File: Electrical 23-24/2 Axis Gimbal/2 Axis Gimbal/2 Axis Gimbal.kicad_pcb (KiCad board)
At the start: 2 copper layers, 29 parts, among them IC1 BNO085, IC2 AP1086DL-13, J1 Conn_01x06_Socket, J2 Conn_01x06_Socket, U1 ATtiny404-SS

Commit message: Starteddddd
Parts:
- removed I2C1: Conn_01x02_Socket, Connector_PinSocket_2.54mm:PinSocket_1x02_P2.54mm_Vertical
- moved IC1 84.3 mm to (92.6, 90.0)
- moved U1 83.8 mm to (92.8, 101.1), turned to 90 degrees
- moved IC2 62.5 mm to (100.8, 111.2), turned to 180 degrees
- moved Power1 29.6 mm to (106.2, 110.5), turned to 180 degrees
- moved XTAL1 25.2 mm to (101.0, 86.8), turned to 90 degrees
- moved J2 22.3 mm to (106.2, 85.4)
- moved Servo2 22.2 mm to (89.6, 113.0), turned to 90 degrees
- moved UART1 19.7 mm to (106.2, 101.8)
- moved Servo1 18.4 mm to (89.6, 109.4), turned to 90 degrees
- moved UDPI1 14.2 mm to (84.0, 106.4), turned to 180 degrees
- moved D-CUP2 14.2 mm to (89.1, 89.5), turned to 90 degrees
- moved D-CUP3 12.7 mm to (93.1, 85.8)
- moved R5 12.7 mm to (88.0, 93.2), turned to 180 degrees
- moved C1 11.9 mm to (87.0, 101.3), turned to 90 degrees
- moved R4 11.6 mm to (92.9, 95.5), turned to 90 degrees
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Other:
- board outline added: 45 x 45 mm

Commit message: Update 2 Axis Gimbal.kicad_pcb
Finished PCB
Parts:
- moved Power1 28.5 mm to (77.9, 107.3)
- moved D1 22.2 mm to (83.2, 85.0)
- moved R3 21.5 mm to (78.2, 83.8), turned to 180 degrees
- moved C5 21.4 mm to (78.2, 94.8)
- moved R55 20.3 mm to (88.5, 86.8), turned to 90 degrees
- moved R4 20.1 mm to (78.2, 81.8), turned to 0 degrees
- moved IC2 18.6 mm to (83.2, 105.0)
- moved J2 17.8 mm to (92.0, 74.7)
- moved R5 17.0 mm to (78.7, 79.0)
- moved R2 16.8 mm to (78.7, 77.5)
- moved D-CUP1 16.2 mm to (86.4, 76.0), turned to 180 degrees
- moved R6 16.0 mm to (87.8, 82.0)
- moved XTAL1 15.7 mm to (89.0, 76.7)
- moved D-CUP2 15.5 mm to (81.5, 76.0), turned to 180 degrees
- moved C3 15.2 mm to (87.0, 79.9)
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- renumbered Servo1 to Serv1, Servo2 to Serv2
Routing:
- net 3.3: track 0.00 -> 90.0 mm, vias 0 -> 10
- net GND: track 0.00 -> 58.8 mm, vias 0 -> 4
- net STAT: track 0.00 -> 32.0 mm, vias 0 -> 2
- net CSN: track 0.00 -> 18.4 mm, vias 0 -> 2
- net SCL: track 0.00 -> 18.1 mm, vias 0 -> 2
- net RST: track 0.00 -> 17.6 mm, vias 0 -> 2
- net SDA: track 0.00 -> 17.0 mm, vias 0 -> 2
- net RX: track 0.00 -> 16.3 mm
- net INT: track 0.00 -> 16.1 mm, vias 0 -> 2
- net +BATT: track 0.00 -> 15.3 mm
- net PWM 2: track 0.00 -> 14.9 mm
- net TX: track 0.00 -> 14.3 mm
- net PWM 1: track 0.00 -> 13.5 mm
- net UPDI: track 0.00 -> 12.2 mm
- net BOOTN: track 0.00 -> 12.1 mm, vias 0 -> 2
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- added copper zone on F.Cu, net (none)
- added copper zone on B.Cu, net GND
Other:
- board size 45 x 45 mm -> 24.2 x 38.5 mm

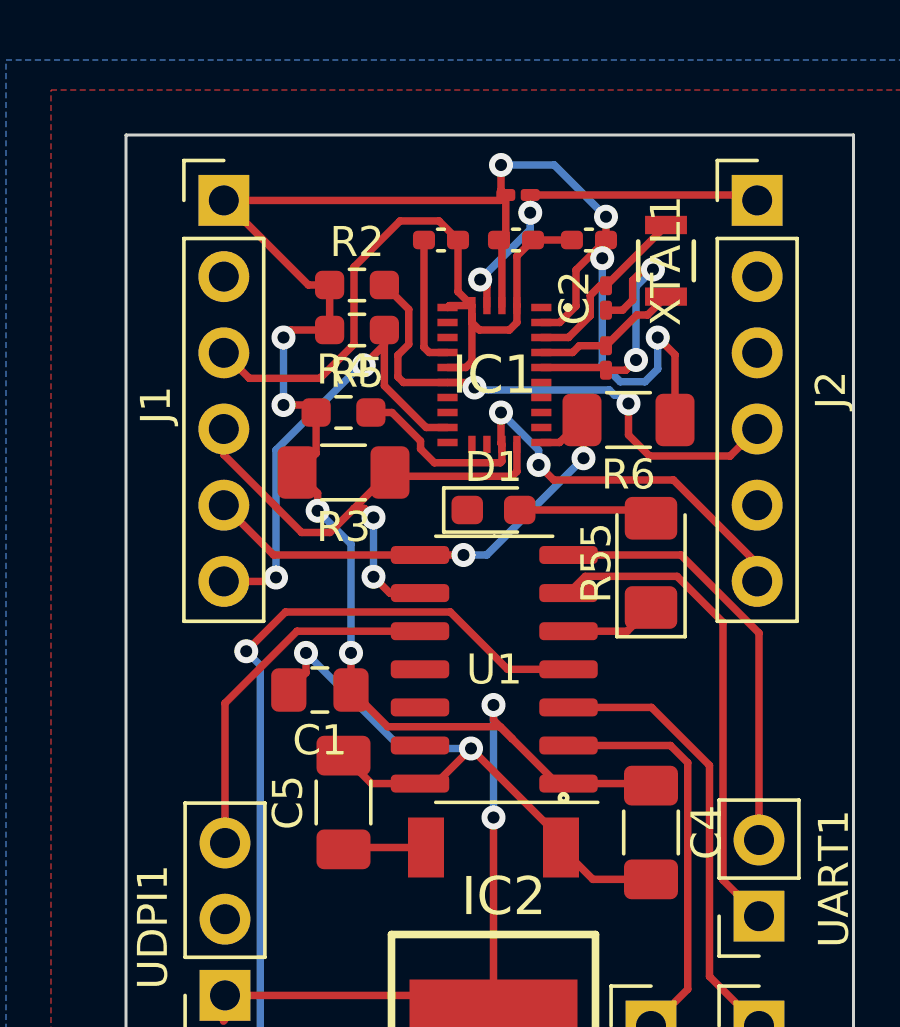
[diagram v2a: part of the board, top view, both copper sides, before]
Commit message: Reformatted PCB
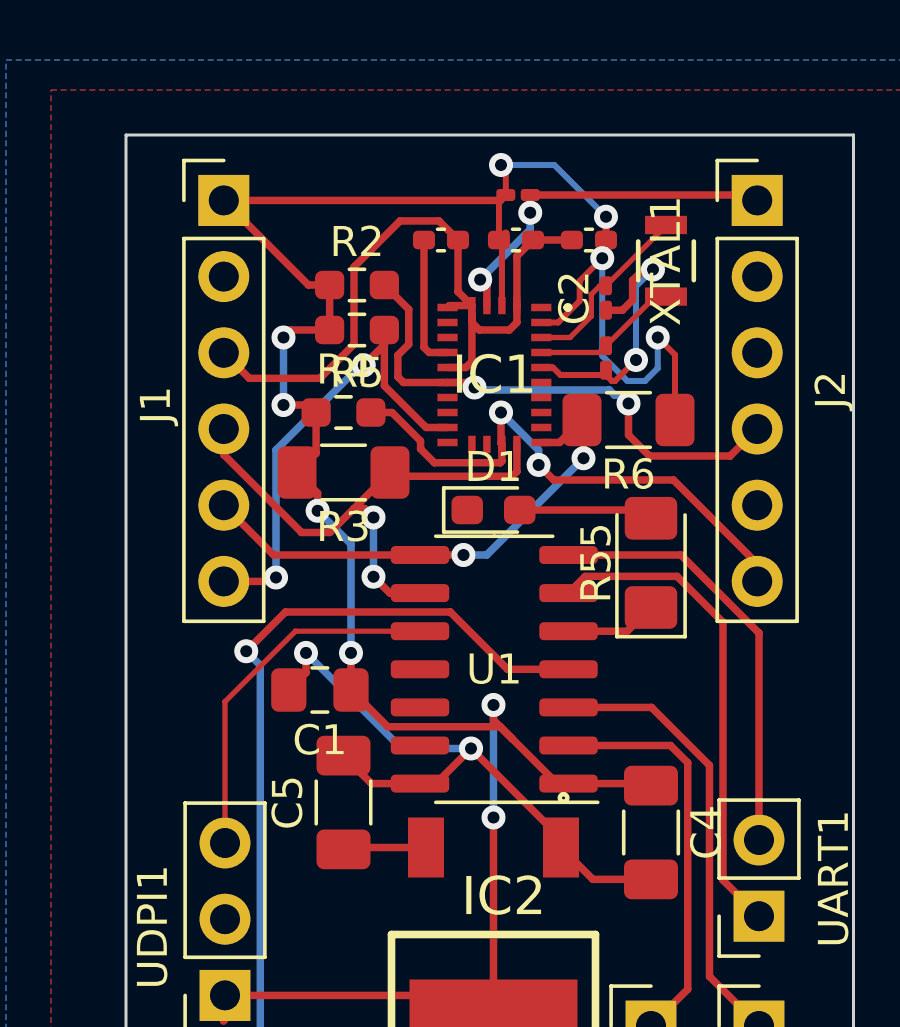
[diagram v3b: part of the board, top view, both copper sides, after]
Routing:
- net GND: track 58.8 -> 59.4 mm
- net 3.3: track 90.0 -> 89.4 mm

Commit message: Finished Gimbal Board
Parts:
- removed the C2 at (87.0, 77.9)
- removed the C3 at (87.0, 79.9)
- removed J1, J2: Conn_01x06_Socket, Connector_PinHeader_2.54mm:PinHeader_1x06_P2.54mm_Vertical
- removed XTAL1: ABS07-32.768KHZ-7-T, 32Crys:XTAL_ABS07-32.768KHZ-7-T_ABR
- added G***: LOGO, LOGO, B.Cu at (108.1, 81.3)
- added R7: 2.2k, Resistor_SMD:R_0603_1608Metric_Pad0.98x0.95mm_HandSolder, F.Cu at (112.9, 85.6)
- added Servo3: Conn_01x03_Pin, Connector_JST:JST_XH_B3B-XH-A_1x03_P2.50mm_Vertical, F.Cu at (91.9, 91.0)
- added U2: ~, gimbal:breakout, F.Cu at (107.4, 81.3)
- C1: value C_10uF -> 10u; footprint Capacitor_SMD:C_0805_2012Metric_Pad1.18x1.45mm_HandSolder -> Capacitor_SMD:C_0603_1608Metric_Pad1.08x0.95mm_HandSolder
- C2: renamed from D-CUP2; value C_0.1uF -> 0.1u; footprint Capacitor_SMD:C_0402_1005Metric_Pad0.74x0.62mm_HandSolder -> Capacitor_SMD:C_0603_1608Metric_Pad1.08x0.95mm_HandSolder
- C3: renamed from D-CUP3; value C_0.1uF -> 0.1u; footprint Capacitor_SMD:C_0402_1005Metric_Pad0.74x0.62mm_HandSolder -> Capacitor_SMD:C_0603_1608Metric_Pad1.08x0.95mm_HandSolder
- C4, C5: value C_100uF -> 10u; footprint Capacitor_SMD:C_1206_3216Metric_Pad1.33x1.80mm_HandSolder -> Capacitor_SMD:C_0603_1608Metric_Pad1.08x0.95mm_HandSolder
- C6: renamed from D-CUP1; value C_0.1uF -> 0.1u; footprint Capacitor_SMD:C_0402_1005Metric_Pad0.74x0.62mm_HandSolder -> Capacitor_SMD:C_0603_1608Metric_Pad1.08x0.95mm_HandSolder
- IC1: footprint BNO085:BNO085 -> gimbal:BNO085
- IC2: footprint VReg3.3:TO252-3L_1 -> gimbal:TO252-3L_1
- Power1, UART1: footprint Connector_PinSocket_2.54mm:PinSocket_1x02_P2.54mm_Vertical -> Connector_JST:JST_XH_B2B-XH-A_1x02_P2.50mm_Vertical
- R1: value 10KR -> 10k; footprint Resistor_SMD:R_0201_0603Metric_Pad0.64x0.40mm_HandSolder -> Resistor_SMD:R_0603_1608Metric_Pad0.98x0.95mm_HandSolder
- R2, R5: value 10KR -> 10k
- R3, R6: footprint Resistor_SMD:R_1206_3216Metric_Pad1.30x1.75mm_HandSolder -> Resistor_SMD:R_0603_1608Metric_Pad0.98x0.95mm_HandSolder
- R4: value 10KR -> 2.2k
- R55: value RES -> 140; footprint LED_SMD:LED_1206_3216Metric_Pad1.42x1.75mm_HandSolder -> Resistor_SMD:R_0603_1608Metric_Pad0.98x0.95mm_HandSolder
- STAT1: footprint Connector_PinHeader_2.54mm:PinHeader_1x02_P2.54mm_Vertical -> Connector_JST:JST_XH_B2B-XH-A_1x02_P2.50mm_Vertical
- Servo1: renamed from Serv1; footprint Connector_PinHeader_2.54mm:PinHeader_1x03_P2.54mm_Vertical -> Connector_JST:JST_XH_B3B-XH-A_1x03_P2.50mm_Vertical
- Servo2: renamed from Serv2; footprint Connector_PinHeader_2.54mm:PinHeader_1x03_P2.54mm_Vertical -> Connector_JST:JST_XH_B3B-XH-A_1x03_P2.50mm_Vertical
- UDPI1: footprint Connector_PinSocket_2.54mm:PinSocket_1x03_P2.54mm_Vertical -> Connector_PinSocket_2.54mm:PinSocket_1x05_P2.54mm_Vertical
- moved C1 36.8 mm to (107.2, 69.3)
- moved R4 34.7 mm to (112.9, 84.1)
- moved Power1 33.3 mm to (78.1, 74.0), turned to 90 degrees
- moved STAT1 32.6 mm to (85.0, 74.0), turned to 90 degrees
- moved IC2 30.7 mm to (110.2, 90.2), turned to -90 degrees
- moved C2 29.7 mm to (110.2, 83.9), turned to 90 degrees
- moved R1 29.5 mm to (113.5, 73.9), turned to -90 degrees
- moved U1 28.4 mm to (106.9, 74.7), turned to 0 degrees
- moved UART1 27.0 mm to (93.0, 71.5), turned to -90 degrees
- moved C4 24.5 mm to (112.8, 92.1)
- moved IC1 23.9 mm to (107.1, 82.1), turned to 180 degrees
- moved C3 23.6 mm to (105.5, 85.8), turned to 180 degrees
- moved R5 23.4 mm to (101.5, 73.7)
- moved R2 22.8 mm to (101.5, 75.9)
- moved UDPI1 22.8 mm to (80.5, 79.2), turned to 90 degrees
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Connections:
- C5 pad 1: +5V -> +BATT
- IC1 pad 10: GND -> 3.3
- IC1 pad 15: unconnected-(IC1-ENV_SCL_-Pad15) -> Net-(IC1-ENV_SCL_)
- IC1 pad 16: unconnected-(IC1-ENV_SDA-Pad16) -> Net-(IC1-ENV_SDA)
- IC1 pad 17: unconnected-(IC1-SA0/H_MOSI_-Pad17) -> GND
- IC1 pad 18: CSN -> unconnected-(IC1-H_CSN-Pad18)
- IC1 pad 26: Net-(IC1-XOUT32/CLKSEL1) -> GND
- IC1 pad 27: Net-(IC1-XIN32) -> unconnected-(IC1-XIN32-Pad27)
- IC2 pad 2: +5V -> +BATT
- R4 pad 1: 3.3 -> Net-(IC1-ENV_SCL_)
- R4 pad 2: CSN -> 3.3
- R55 pad 1: LED -> STAT
- U1 pad 11: unconnected-(U1-PA1-Pad11) -> BOOTN
- U1 pad 12: unconnected-(U1-PA2-Pad12) -> INT
- U1 pad 13: unconnected-(U1-PA3-Pad13) -> PWM 1
- U1 pad 2: PWM 1 -> PWM 2
- U1 pad 3: PWM 2 -> PWM 3
- U1 pad 5: LED -> RST
- UDPI1 pad 1: 3.3 -> UPDI
- UDPI1 pad 2: GND -> 3.3
- UDPI1 pad 3: UPDI -> GND
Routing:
- net GND: track 59.4 -> 156.2 mm, vias 4 -> 13
- net PWM 3: track 0.00 -> 53.1 mm
- net PWM 1: track 13.5 -> 56.9 mm
- net 3.3: track 89.4 -> 130.9 mm, vias 10 -> 2
- net PWM 2: track 14.9 -> 51.9 mm
- net +BATT: track 15.3 -> 42.4 mm
- net INT: track 16.1 -> 38.3 mm, vias 2 -> 4
- net UPDI: track 12.2 -> 34.1 mm
- net CSN: track 18.4 -> 0.00 mm, vias 2 -> 0
- net BOOTN: track 12.1 -> 24.7 mm
- net Net-(IC1-ENV_SDA): track 0.00 -> 9.91 mm, vias 0 -> 2
- net RX: track 16.3 -> 25.6 mm
- net TX: track 14.3 -> 22.2 mm
- net Net-(IC1-ENV_SCL_): track 0.00 -> 6.44 mm, vias 0 -> 2
- net Net-(IC1-XIN32): track 6.15 -> 0.00 mm
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- added copper zone on F.Cu, net GND
- removed copper zone on F.Cu, net (none)
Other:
- board size 24.2 x 38.5 mm -> 44.5 x 26.4 mm
- board text added: "1"
- board text added: "2"
- board text added: "3"
- board text added: "3V3"
- board text added: "3V3 REG"
- board text added: "3VO"
- board text added: "ATTINY404"
- board text added: "Anthony Cheung Ari Bobesh"
- board text added: "BNO086"
- board text added: "BOOT"
- board text added: "CS"
- board text added: "DI"
- board text added: "GND"
- board text added: "Gimbal Board V1 04/02/24"
- board text added: "INT"
- board text added: "P0"
- board text added: "P1"
- board text added: "POWER"
- board text added: "PWM"
- board text added: "RST"
- board text added: "RX"
- board text added: "SCL"
- board text added: "SDA"
- board text added: "SERVOS"
- board text added: "STAT"
- board text added: "TX"
- board text added: "UART"
- board text added: "UPDI 3V3 GND RX TX"
- board text added: "VBAT"

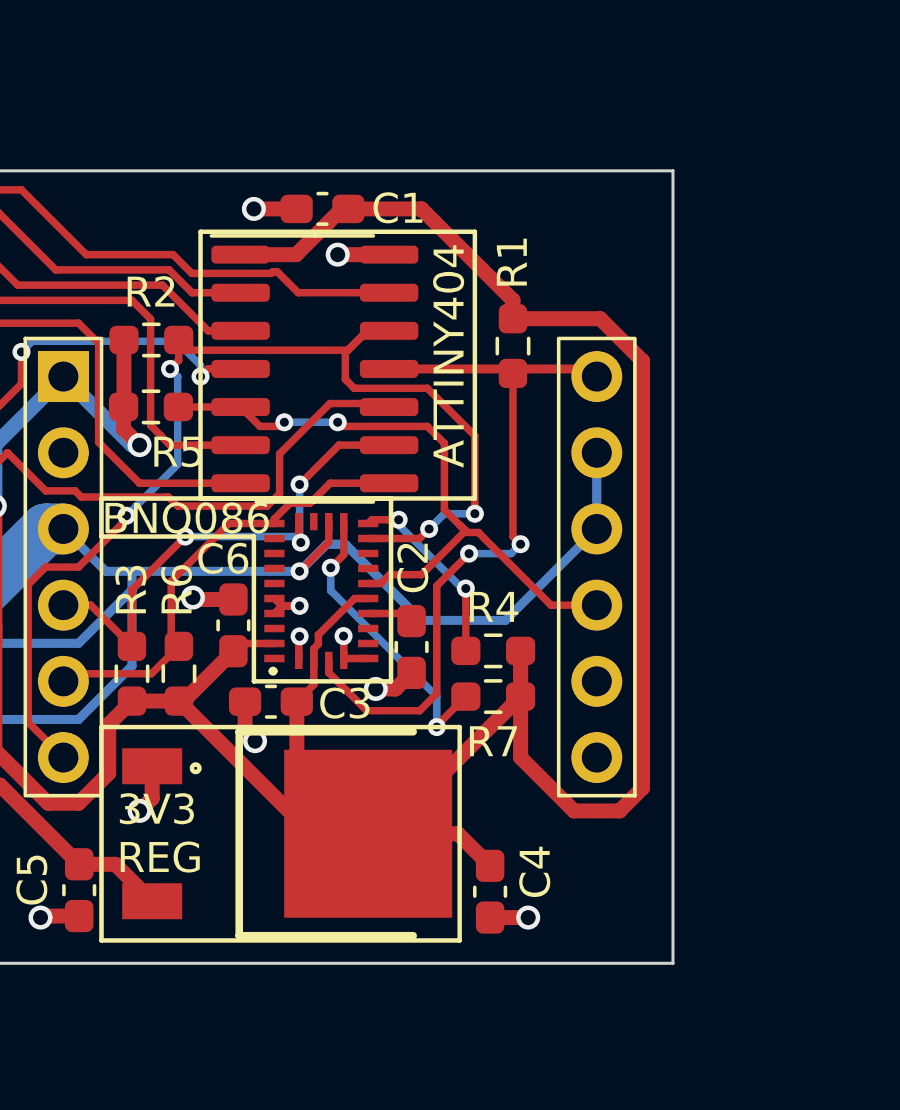
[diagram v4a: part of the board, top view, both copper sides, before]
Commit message: Add JLC Serial # Location to All
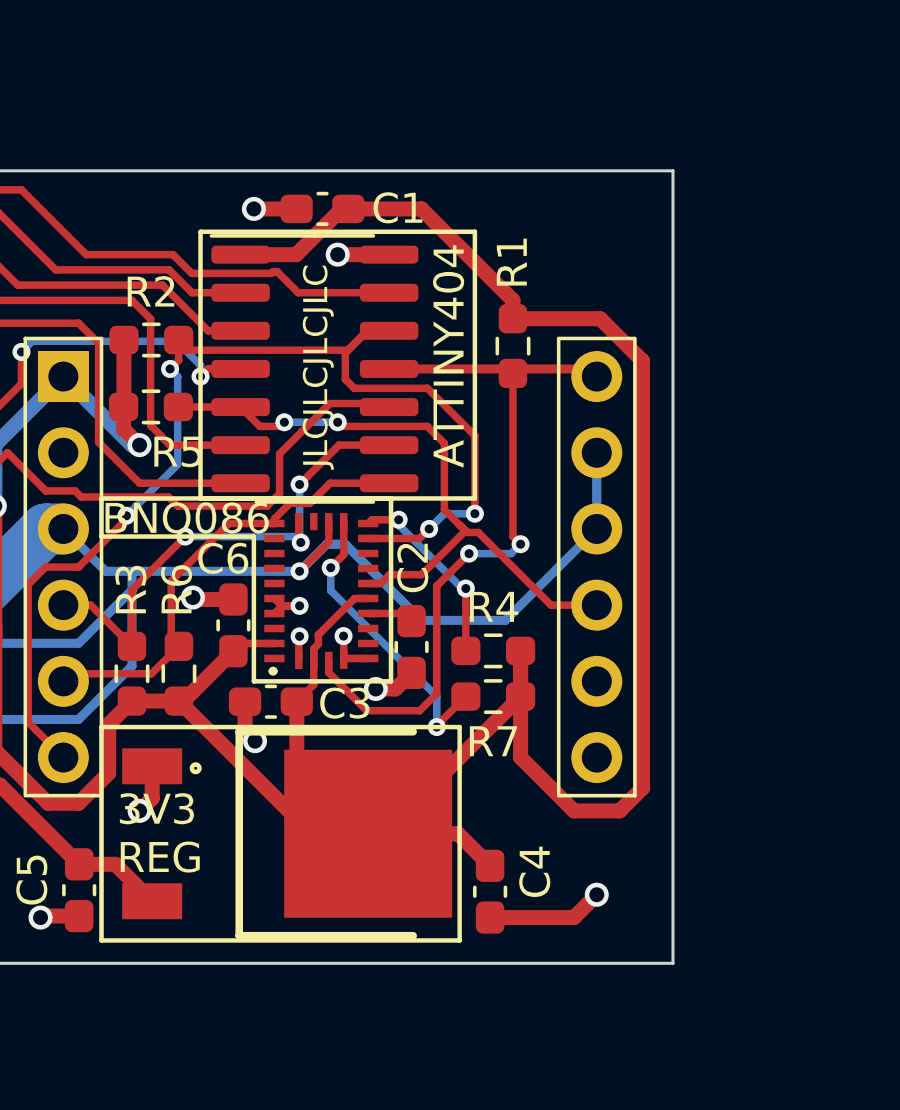
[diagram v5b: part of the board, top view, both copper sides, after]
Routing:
- net GND: track 156.2 -> 158.8 mm
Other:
- board text added: "JLCJLCJLCJLC"

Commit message: Fix a MAJOR issue that ANTHONY caused
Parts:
- added R8: 2.2k, Resistor_SMD:R_0603_1608Metric_Pad0.98x0.95mm_HandSolder, F.Cu at (99.4, 90.4)
- added R9: 3.6k, Resistor_SMD:R_0603_1608Metric_Pad0.98x0.95mm_HandSolder, F.Cu at (99.4, 91.9)
- moved C5 2.73 mm to (96.3, 92.0)
- moved C4 1.37 mm to (114.2, 92.1)
- moved IC2 1.04 mm to (111.2, 90.2)
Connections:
- IC2 pad 1: GND -> Net-(IC2-ADJ_(GND))
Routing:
- net 3.3: track 130.9 -> 122.4 mm
- net Net-(IC2-ADJ_(GND)): track 0.00 -> 4.91 mm
- net +BATT: track 42.4 -> 44.5 mm
- net GND: track 158.8 -> 157.2 mm
